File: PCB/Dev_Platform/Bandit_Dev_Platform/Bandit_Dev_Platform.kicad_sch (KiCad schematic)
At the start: 136 parts, among them J1 Conn_01x03_Pin, J10 Conn_01x05_Pin, J11 Conn_01x05_Pin, J2 SMA, J3 Conn_01x05_Pin, J4 Conn_01x05_Pin, J5 BNC, J6 BNC, J7 SMA, J8 Conn_01x05_Pin, J9 Conn_01x06_Pin, P1 USB_C_Plug_USB2.0, SW1 SW_SPST, U1 AD7253, U1 OPA1664, U2 RP2040, U3 AP2210N-4.0TRG1, U4 NCP164ASNADJT1G, U5 W25Q16JVUXIQ_TR, U6 MCP6486UT-E/OT, U7 MCP6S92-E/SN, U8 MIC5504-3.3YM5, X1 SG-210STF, Y1 12.000 MHz, C9002

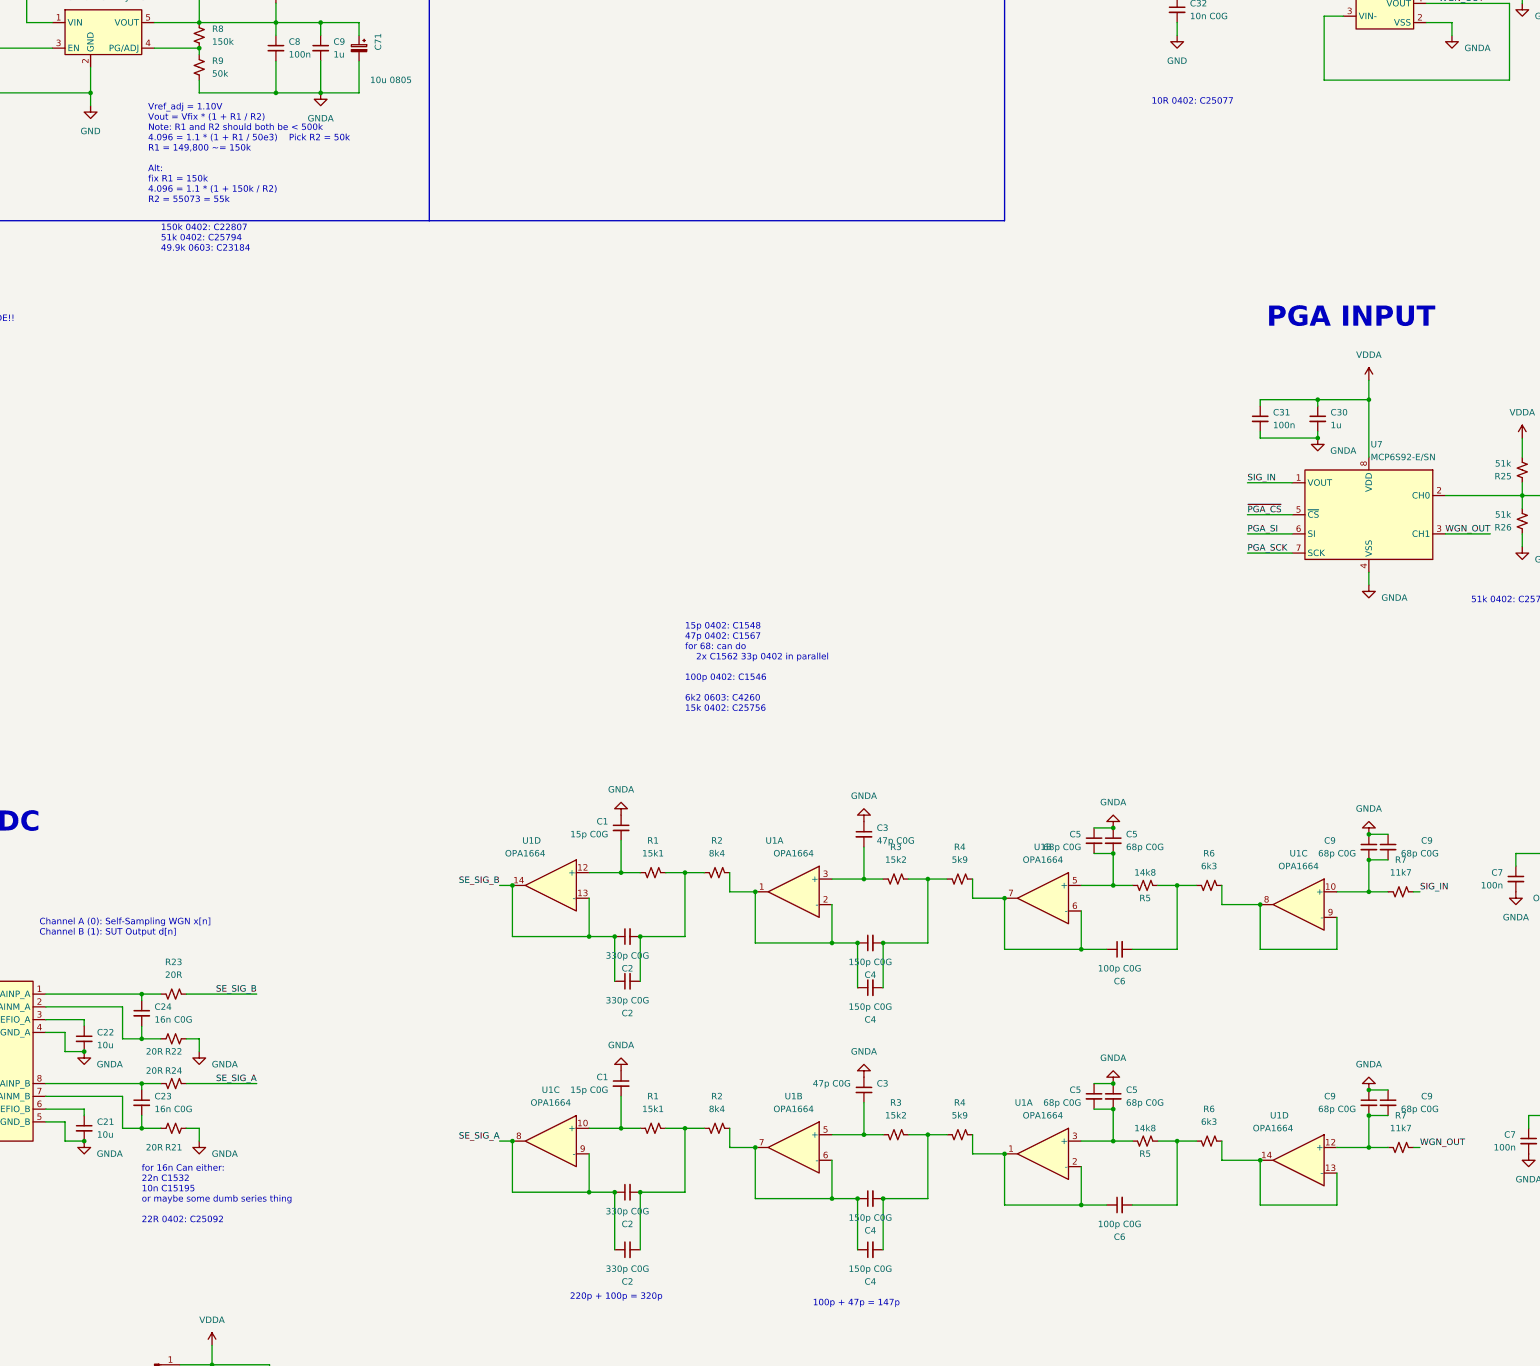
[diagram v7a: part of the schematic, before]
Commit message: Fixed filter to be cheap
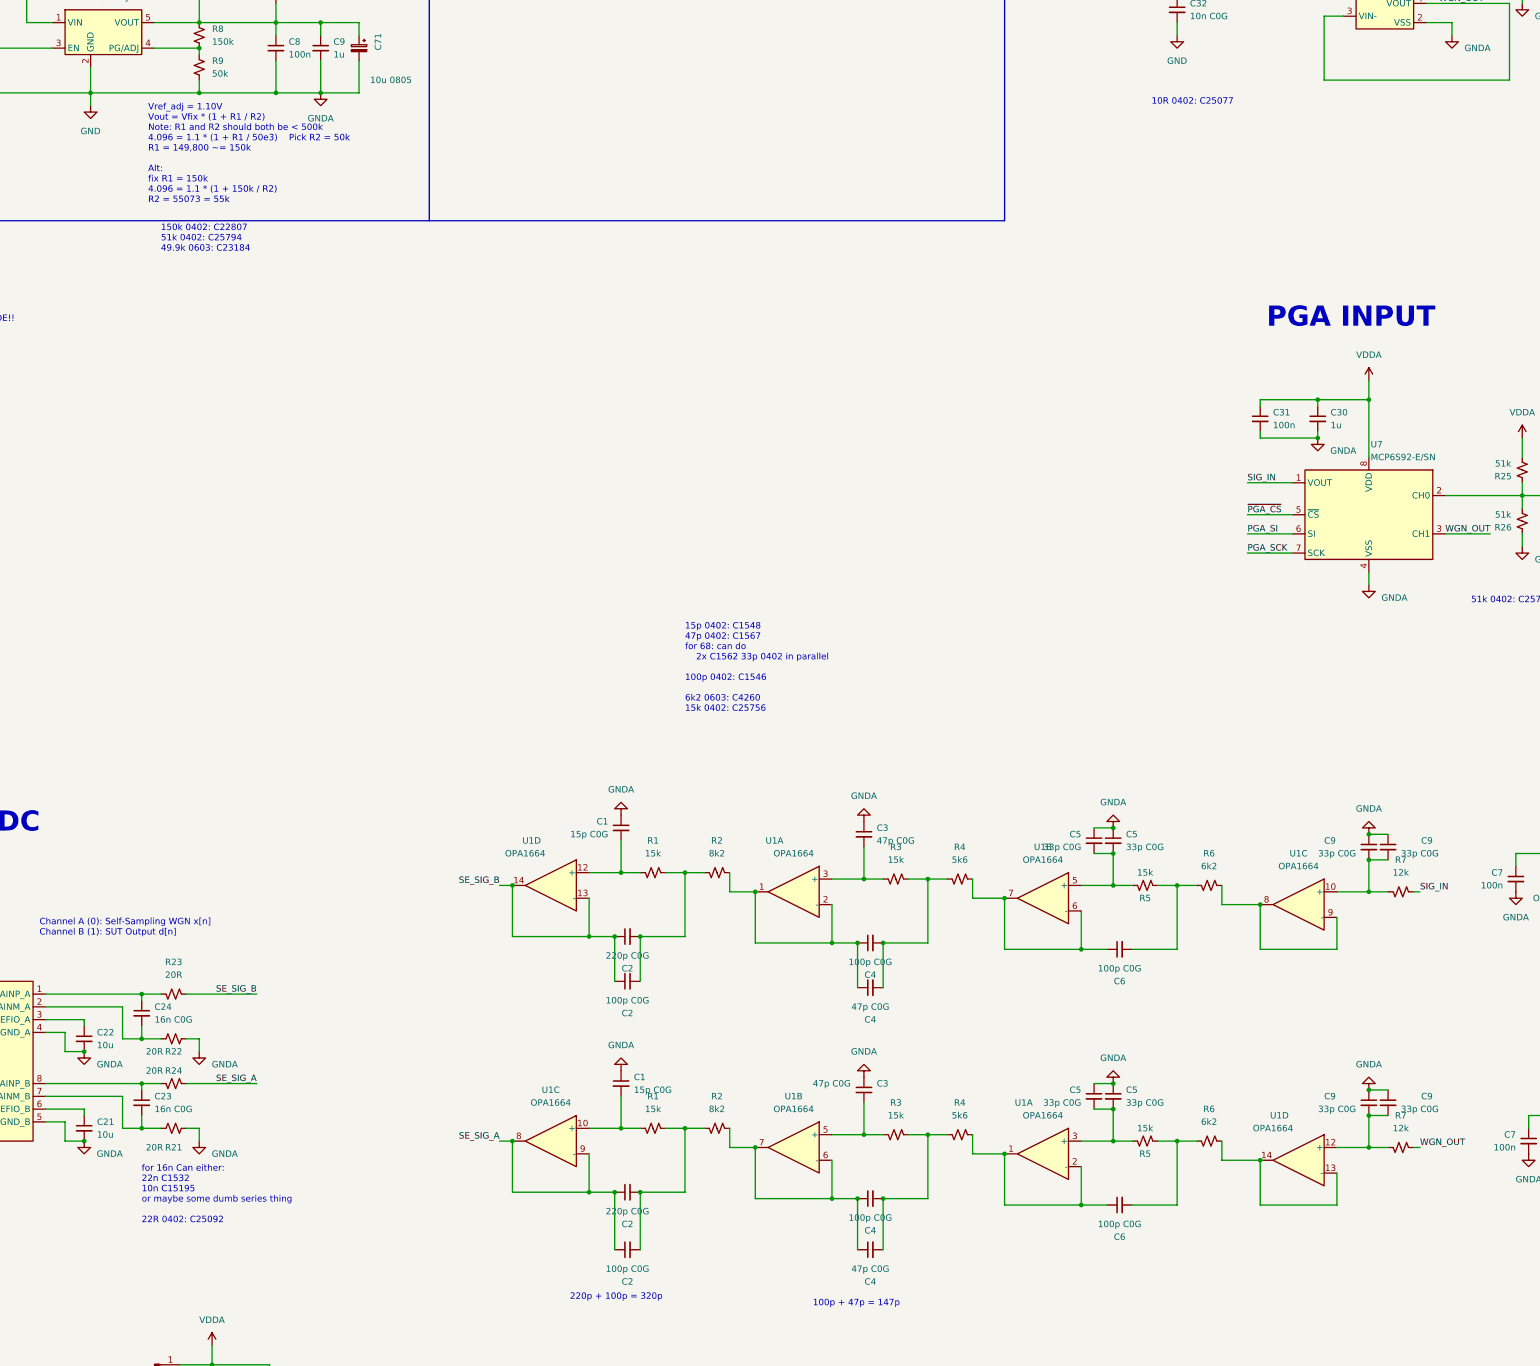
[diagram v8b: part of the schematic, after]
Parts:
- C2: value 330p C0G -> 100p C0G
- C2: value 330p C0G -> 220p C0G
- C4: value 150p C0G -> 100p C0G
- C4: value 150p C0G -> 47p C0G
- C5, C9: value 68p C0G -> 33p C0G
- R1: value 15k1 -> 15k; footprint Resistor_SMD:R_0603_1608Metric -> Resistor_SMD:R_0402_1005Metric
- R2: value 8k4 -> 8k2
- R3: value 15k2 -> 15k
- R4: value 5k9 -> 5k6
- R5: value 14k8 -> 15k; footprint Resistor_SMD:R_0603_1608Metric -> Resistor_SMD:R_0402_1005Metric
- R6: value 6k3 -> 6k2
- R7: value 11k7 -> 12k; footprint Resistor_SMD:R_0603_1608Metric -> Resistor_SMD:R_0402_1005Metric
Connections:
- net GNDA is gone; now on net GND: C1.1, C1.1, C12.2, C13.2, C14.2, C15.2, C21.2, C22.2, C26.2, C27.2, C3.1, C3.1, C30.2, C31.2, C5.1, C5.1, C5.1, C5.1, C7.2, C7.2, C71.2, C8.2, C8.2, C8.2, C9.1, C9.1, C9.1, C9.1, C9.2, J10.1 (Pin_1), J10.2 (Pin_2), J10.4 (Pin_4), J10.5 (Pin_5), J11.4 (Pin_4), J11.5 (Pin_5), J2.2 (Ext), J3.1 (Pin_1), J3.2 (Pin_2), J3.4 (Pin_4), J3.5 (Pin_5), J4.4 (Pin_4), J4.5 (Pin_5), J5.2 (Ext), J6.2 (Ext), J7.2 (Ext), R21.1, R24.1, R26.2, R9.1, U1.11 (V-), U1.11 (V-), U1.4 (REFGND_A), U1.5 (REFGND_B), U6.2 (VSS), U7.4 (VSS)
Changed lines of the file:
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@@
   (junction (at 245.11 274.32) (diameter 0) (color 0 0 0 0)
   )
+  (junction (at 256.54 86.36) (diameter 0) (color 0 0 0 0)
+  )
   (junction (at 353.06 241.3) (diameter 0) (color 0 0 0 0)
   )
@@
     (stroke (width 0) (type default))
   )
+  (wire (pts (xy 234.95 86.36) (xy 256.54 86.36))
+    (stroke (width 0) (type default))
+  )
   (wire (pts (xy 382.27 298.45) (xy 382.27 306.07))
     (stroke (width 0) (type default))
@@
       (effects (font (size 1.27 1.27)))
     )
-    (property "Value" "15k2" (at 394.97 238.76 90)
+    (property "Value" "15k" (at 394.97 238.76 90)
       (effects (font (size 1.27 1.27)))
     )
@@
       (effects (font (size 1.27 1.27)))
     )
-    (property "Value" "5k9" (at 407.67 238.76 90)
+    (property "Value" "5k6" (at 407.67 238.76 90)
       (effects (font (size 1.27 1.27)))
     )
@@
       (effects (font (size 1.27 1.27)))
     )
-    (property "Value" "330p	C0G" (at 341.6364 320.04 90)
+    (property "Value" "100p	C0G" (at 341.6364 320.04 90)
       (effects (font (size 1.27 1.27)))
     )
@@
       (effects (font (size 1.27 1.27)) (justify right))
     )
-    (property "Value" "68p	C0G" (at 431.8 236.2263 0)
+    (property "Value" "33p	C0G" (at 431.8 236.2263 0)
       (effects (font (size 1.27 1.27)) (justify right))
     )
@@
       (effects (font (size 1.27 1.27)))
     )
-    (property "Value" "150p	C0G" (at 389.8964 259.08 90)
+    (property "Value" "100p	C0G" (at 389.8964 259.08 90)
       (effects (font (size 1.27 1.27)))
     )
@@
       (effects (font (size 1.27 1.27)))
     )
-    (property "Value" "15k1" (at 346.71 288.29 90)
+    (property "Value" "15k" (at 346.71 288.29 90)
       (effects (font (size 1.27 1.27)))
     )
-    (property "Footprint" "Resistor_SMD:R_0603_1608Metric" (at 346.71 292.1 0)
+    (property "Footprint" "Resistor_SMD:R_0402_1005Metric" (at 346.71 292.1 0)
       (effects (font (size 1.27 1.27)) hide)
     )
@@
       (effects (font (size 1.27 1.27)))
     )
-    (property "Value" "150p	C0G" (at 389.8964 320.04 90)
+    (property "Value" "47p	C0G" (at 389.8964 320.04 90)
       (effects (font (size 1.27 1.27)))
     )
@@
       (effects (font (size 1.27 1.27)) (justify right))
     )
-    (property "Value" "68p	C0G" (at 440.69 287.0263 0)
+    (property "Value" "33p	C0G" (at 440.69 287.0263 0)
       (effects (font (size 1.27 1.27)) (justify right))
     )
@@
       (effects (font (size 1.27 1.27)))
     )
-    (property "Value" "8k4" (at 359.41 237.49 90)
+    (property "Value" "8k2" (at 359.41 237.49 90)
       (effects (font (size 1.27 1.27)))
     )
@@
       (effects (font (size 1.27 1.27)))
     )
-    (property "Value" "15k2" (at 394.97 289.56 90)
+    (property "Value" "15k" (at 394.97 289.56 90)
       (effects (font (size 1.27 1.27)))
     )
@@
       (effects (font (size 1.27 1.27)))
     )
-    (property "Value" "150p	C0G" (at 389.8964 309.88 90)
+    (property "Value" "100p	C0G" (at 389.8964 309.88 90)
       (effects (font (size 1.27 1.27)))
     )
@@
       (effects (font (size 1.27 1.27)))
     )
-    (property "Value" "150p	C0G" (at 389.8964 267.97 90)
+    (property "Value" "47p	C0G" (at 389.8964 267.97 90)
       (effects (font (size 1.27 1.27)))
     )
@@
       (effects (font (size 1.27 1.27)))
     )
-    (property "Value" "6k3" (at 457.2 290.83 90)
+    (property "Value" "6k2" (at 457.2 290.83 90)
       (effects (font (size 1.27 1.27)))
     )
@@
       (effects (font (size 1.27 1.27)))
     )
-    (property "Value" "5k9" (at 407.67 289.56 90)
+    (property "Value" "5k6" (at 407.67 289.56 90)
       (effects (font (size 1.27 1.27)))
     )
@@
       (effects (font (size 1.27 1.27)) (justify right))
     )
-    (property "Value" "68p	C0G" (at 431.8 287.0263 0)
+    (property "Value" "33p	C0G" (at 431.8 287.0263 0)
       (effects (font (size 1.27 1.27)) (justify right))
     )
@@
       (effects (font (size 1.27 1.27)) (justify right))
     )
-    (property "Value" "68p	C0G" (at 440.69 236.2263 0)
+    (property "Value" "33p	C0G" (at 440.69 236.2263 0)
       (effects (font (size 1.27 1.27)) (justify right))
     )
@@
       (effects (font (size 1.27 1.27)))
     )
-    (property "Value" "330p	C0G" (at 341.6364 257.81 90)
+    (property "Value" "220p	C0G" (at 341.6364 257.81 90)
       (effects (font (size 1.27 1.27)))
     )
@@
       (effects (font (size 1.27 1.27)))
     )
-    (property "Value" "15k1" (at 346.71 237.49 90)
+    (property "Value" "15k" (at 346.71 237.49 90)
       (effects (font (size 1.27 1.27)))
     )
-    (property "Footprint" "Resistor_SMD:R_0603_1608Metric" (at 346.71 241.3 0)
+    (property "Footprint" "Resistor_SMD:R_0402_1005Metric" (at 346.71 241.3 0)
       (effects (font (size 1.27 1.27)) hide)
     )
@@
       (effects (font (size 1.27 1.27)) (justify right))
     )
-    (property "Value" "68p C0G" (at 495.3 288.29 0)
+    (property "Value" "33p C0G" (at 495.3 288.29 0)
       (effects (font (size 1.27 1.27)) (justify left))
     )
@@
       (effects (font (size 1.27 1.27)))
     )
-    (property "Value" "14k8" (at 444.5 292.1 90)
+    (property "Value" "15k" (at 444.5 292.1 90)
       (effects (font (size 1.27 1.27)))
     )
-    (property "Footprint" "Resistor_SMD:R_0603_1608Metric" (at 444.5 294.64 0)
+    (property "Footprint" "Resistor_SMD:R_0402_1005Metric" (at 444.5 294.64 0)
       (effects (font (size 1.27 1.27)) hide)
     )
@@
       (effects (font (size 1.27 1.27)))
     )
-    (property "Value" "330p	C0G" (at 341.6364 308.61 90)
+    (property "Value" "220p C0G" (at 341.6364 308.61 90)
       (effects (font (size 1.27 1.27)))
     )
@@
       (effects (font (size 1.27 1.27)) (justify right))
     )
-    (property "Value" "68p C0G" (at 495.3 237.49 0)
+    (property "Value" "33p C0G" (at 495.3 237.49 0)
       (effects (font (size 1.27 1.27)) (justify left))
     )
@@
       (effects (font (size 1.27 1.27)))
     )
-    (property "Value" "6k3" (at 457.2 240.03 90)
+    (property "Value" "6k2" (at 457.2 240.03 90)
       (effects (font (size 1.27 1.27)))
     )
@@
   (symbol (lib_id "Device:C_Small") (at 340.36 283.21 0) (mirror y) (unit 1)
     (in_bom yes) (on_board yes) (dnp no) (fields_autoplaced)
-    (property "Reference" "C1" (at 337.82 281.9463 0)
-      (effects (font (size 1.27 1.27)) (justify left))
+    (property "Reference" "C1" (at 342.9 281.9463 0)
+      (effects (font (size 1.27 1.27)) (justify right))
     )
-    (property "Value" "15p   C0G" (at 337.82 284.4863 0)
-      (effects (font (size 1.27 1.27)) (justify left))
+    (property "Value" "15p   C0G" (at 342.9 284.4863 0)
+      (effects (font (size 1.27 1.27)) (justify right))
     )
     (property "Footprint" "Capacitor_SMD:C_0402_1005Metric" (at 340.36 283.21 0)
@@
       (effects (font (size 1.27 1.27)) (justify right))
     )
-    (property "Value" "68p C0G" (at 486.41 237.49 0)
+    (property "Value" "33p C0G" (at 486.41 237.49 0)
       (effects (font (size 1.27 1.27)) (justify left))
     )
@@
       (effects (font (size 1.27 1.27)))
     )
-    (property "Value" "11k7" (at 495.3 292.1 90)
+    (property "Value" "12k" (at 495.3 292.1 90)
       (effects (font (size 1.27 1.27)))
     )
-    (property "Footprint" "Resistor_SMD:R_0603_1608Metric" (at 495.3 295.91 0)
+    (property "Footprint" "Resistor_SMD:R_0402_1005Metric" (at 495.3 295.91 0)
       (effects (font (size 1.27 1.27)) hide)
     )
@@
       (effects (font (size 1.27 1.27)))
     )
-    (property "Value" "330p	C0G" (at 341.6364 266.7 90)
+    (property "Value" "100p	C0G" (at 341.6364 266.7 90)
       (effects (font (size 1.27 1.27)))
     )
@@
       (effects (font (size 1.27 1.27)))
     )
-    (property "Value" "14k8" (at 444.5 241.3 90)
+    (property "Value" "15k" (at 444.5 241.3 90)
       (effects (font (size 1.27 1.27)))
     )
-    (property "Footprint" "Resistor_SMD:R_0603_1608Metric" (at 444.5 243.84 0)
+    (property "Footprint" "Resistor_SMD:R_0402_1005Metric" (at 444.5 243.84 0)
       (effects (font (size 1.27 1.27)) hide)
     )
@@
       (effects (font (size 1.27 1.27)) (justify right))
     )
-    (property "Value" "68p C0G" (at 486.41 288.29 0)
+    (property "Value" "33p C0G" (at 486.41 288.29 0)
       (effects (font (size 1.27 1.27)) (justify left))
     )
@@
       (effects (font (size 1.27 1.27)))
     )
-    (property "Value" "8k4" (at 359.41 288.29 90)
+    (property "Value" "8k2" (at 359.41 288.29 90)
       (effects (font (size 1.27 1.27)))
     )
@@
       (effects (font (size 1.27 1.27)))
     )
-    (property "Value" "11k7" (at 495.3 241.3 90)
+    (property "Value" "12k" (at 495.3 241.3 90)
       (effects (font (size 1.27 1.27)))
     )
-    (property "Footprint" "Resistor_SMD:R_0603_1608Metric" (at 495.3 245.11 0)
+    (property "Footprint" "Resistor_SMD:R_0402_1005Metric" (at 495.3 245.11 0)
       (effects (font (size 1.27 1.27)) hide)
     )
